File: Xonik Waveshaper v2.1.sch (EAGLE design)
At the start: 89 parts, among them IC1 TL074D, IC2 TL074D, IC3 TL074D, IC4 TL072D, IC5 4013D, T1 2n3904

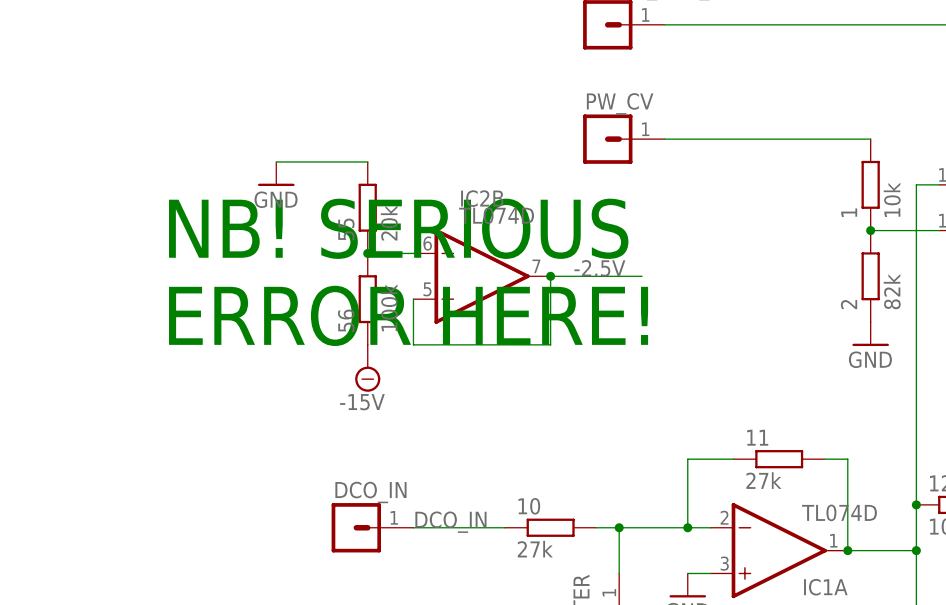
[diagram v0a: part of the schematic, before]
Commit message: v2.1 - fixed serious bug, had mixed up + and - on -2.5v generator op amp
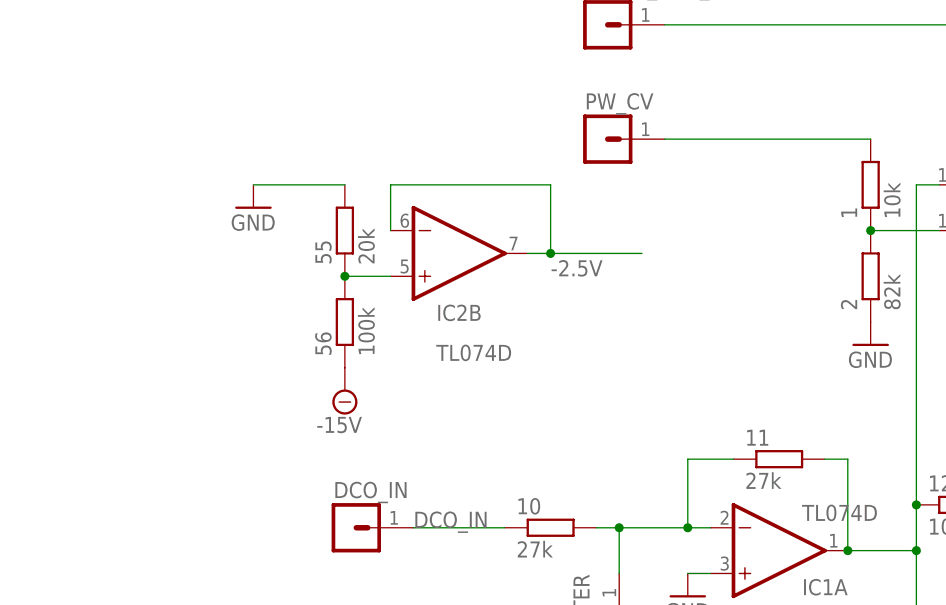
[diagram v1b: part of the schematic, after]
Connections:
- net -2.5V: now also IC2B.-IN; no longer IC2B.+IN
- net N$33: now also IC2B.+IN; no longer IC2B.-IN
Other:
- note removed: "NB! SERIOUS ERROR HERE!"
- moved on the sheet: 55, 56, IC2B
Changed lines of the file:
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@@
 <text x="-48.26" y="111.76" size="1.778" layer="97">PW is about 6% of the total cycle at the narrowest.
 Change R2 to 150 to reduce to half that.</text>
-<text x="-83.82" y="68.58" size="6.4516" layer="91">NB! SERIOUS
-ERROR HERE!</text>
 </plain>
 <instances>
@@
 <attribute name="VALUE" x="25.4" y="-81.28" size="1.778" layer="96" rot="MR180"/>
 </instance>
-<instance part="IC2" gate="B" x="-48.26" y="76.2" smashed="yes" rot="MR180">
-<attribute name="NAME" x="-50.8" y="85.725" size="1.778" layer="95" rot="MR180"/>
-<attribute name="VALUE" x="-50.8" y="83.82" size="1.778" layer="96" rot="MR180"/>
+<instance part="IC2" gate="B" x="-50.8" y="78.74" smashed="yes" rot="MR180">
+<attribute name="NAME" x="-53.34" y="73.025" size="1.778" layer="95" rot="MR180"/>
+<attribute name="VALUE" x="-53.34" y="68.58" size="1.778" layer="96" rot="MR180"/>
 </instance>
 <instance part="IC4" gate="B" x="22.86" y="-20.32" smashed="yes" rot="MR180">
@@
 <attribute name="VALUE" x="53.34" y="-114.3" size="1.778" layer="96"/>
 </instance>
-<instance part="55" gate="G$1" x="-60.96" y="83.82" smashed="yes" rot="R90">
-<attribute name="NAME" x="-62.4586" y="80.01" size="1.778" layer="95" rot="R90"/>
-<attribute name="VALUE" x="-57.658" y="80.01" size="1.778" layer="96" rot="R90"/>
-</instance>
-<instance part="56" gate="G$1" x="-60.96" y="73.66" smashed="yes" rot="R90">
-<attribute name="NAME" x="-62.4586" y="69.85" size="1.778" layer="95" rot="R90"/>
-<attribute name="VALUE" x="-57.658" y="69.85" size="1.778" layer="96" rot="R90"/>
-</instance>
-<instance part="SUPPLY2" gate="G$1" x="-60.96" y="66.04" smashed="yes">
-<attribute name="VALUE" x="-64.135" y="61.341" size="1.778" layer="96"/>
-</instance>
-<instance part="GND14" gate="1" x="-71.12" y="86.36" smashed="yes">
-<attribute name="VALUE" x="-73.66" y="83.82" size="1.778" layer="96"/>
+<instance part="55" gate="G$1" x="-63.5" y="81.28" smashed="yes" rot="R90">
+<attribute name="NAME" x="-64.9986" y="77.47" size="1.778" layer="95" rot="R90"/>
+<attribute name="VALUE" x="-60.198" y="77.47" size="1.778" layer="96" rot="R90"/>
+</instance>
+<instance part="56" gate="G$1" x="-63.5" y="71.12" smashed="yes" rot="R90">
+<attribute name="NAME" x="-64.9986" y="67.31" size="1.778" layer="95" rot="R90"/>
+<attribute name="VALUE" x="-60.198" y="67.31" size="1.778" layer="96" rot="R90"/>
+</instance>
+<instance part="SUPPLY2" gate="G$1" x="-63.5" y="63.5" smashed="yes">
+<attribute name="VALUE" x="-66.675" y="58.801" size="1.778" layer="96"/>
+</instance>
+<instance part="GND14" gate="1" x="-73.66" y="83.82" smashed="yes">
+<attribute name="VALUE" x="-76.2" y="81.28" size="1.778" layer="96"/>
 </instance>
 <instance part="IC5" gate="A" x="-35.56" y="-17.78" smashed="yes">
@@
 <pinref part="GND14" gate="1" pin="GND"/>
 <pinref part="55" gate="G$1" pin="2"/>
-<wire x1="-71.12" y1="88.9" x2="-60.96" y2="88.9" width="0.1524" layer="91"/>
+<wire x1="-73.66" y1="86.36" x2="-63.5" y2="86.36" width="0.1524" layer="91"/>
 </segment>
 <segment>
@@
 </segment>
 <segment>
-<pinref part="IC2" gate="B" pin="+IN"/>
-<wire x1="-55.88" y1="73.66" x2="-55.88" y2="68.58" width="0.1524" layer="91"/>
 <pinref part="IC2" gate="B" pin="OUT"/>
-<wire x1="-55.88" y1="68.58" x2="-40.64" y2="68.58" width="0.1524" layer="91"/>
-<wire x1="-40.64" y1="68.58" x2="-40.64" y2="76.2" width="0.1524" layer="91"/>
-<wire x1="-40.64" y1="76.2" x2="-30.48" y2="76.2" width="0.1524" layer="91"/>
-<junction x="-40.64" y="76.2"/>
-<label x="-38.1" y="76.2" size="1.778" layer="95"/>
+<wire x1="-43.18" y1="78.74" x2="-40.64" y2="78.74" width="0.1524" layer="91"/>
+<label x="-40.64" y="76.2" size="1.778" layer="95"/>
+<pinref part="IC2" gate="B" pin="-IN"/>
+<wire x1="-40.64" y1="78.74" x2="-30.48" y2="78.74" width="0.1524" layer="91"/>
+<wire x1="-58.42" y1="81.28" x2="-58.42" y2="86.36" width="0.1524" layer="91"/>
+<wire x1="-58.42" y1="86.36" x2="-40.64" y2="86.36" width="0.1524" layer="91"/>
+<wire x1="-40.64" y1="86.36" x2="-40.64" y2="78.74" width="0.1524" layer="91"/>
+<junction x="-40.64" y="78.74"/>
 </segment>
 </net>
@@
 <pinref part="55" gate="G$1" pin="1"/>
 <pinref part="56" gate="G$1" pin="2"/>
-<pinref part="IC2" gate="B" pin="-IN"/>
-<wire x1="-55.88" y1="78.74" x2="-60.96" y2="78.74" width="0.1524" layer="91"/>
-<junction x="-60.96" y="78.74"/>
-</segment>
-</net>
+<pinref part="IC2" gate="B" pin="+IN"/>
+<wire x1="-58.42" y1="76.2" x2="-63.5" y2="76.2" width="0.1524" layer="91"/>
+<junction x="-63.5" y="76.2"/>
+</segment>
+</net>

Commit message: Replaced 1.5k R19 with 1.2k for a sine closer to +/-5v
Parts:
- 19: value 1k5 -> 1k2
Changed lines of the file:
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@@
 <part name="17" library="resistor" deviceset="R-EU_" device="R0805" value="200k"/>
 <part name="18" library="resistor" deviceset="R-EU_" device="R0805" value="150k"/>
-<part name="19" library="resistor" deviceset="R-EU_" device="R0805" value="1k5"/>
+<part name="19" library="resistor" deviceset="R-EU_" device="R0805" value="1k2"/>
 <part name="20" library="resistor" deviceset="R-EU_" device="R0805" value="15k"/>
 <part name="22" library="resistor" deviceset="R-EU_" device="R0805" value="22k"/>

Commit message: will remove resistor divider
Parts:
- added -2.5V: (no value), joakim:MA01-1JP
- added 9: 50k, resistor:R-EU_R0805
- 55: value 20k -> 100k
- 56: value 100k -> 240k
- renumbered +15V to +12V, -15V to -12V
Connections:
- net +15V renamed +12V
- net -15V renamed -12V
- removed net PW_CV: 1.2, PW_CV.1
- new net N$25: 1.2, 55.2, IC2B.OUT
- new net N$8: 55.1, 56.2, 9.1, IC2B.-IN
- net -2.5V: now also -2.5V.1; no longer IC2B.-IN, IC2B.OUT
- net GND: now also IC2B.+IN; no longer 55.2
- net N$33: now also 9.2, PW_CV.1; no longer 55.1, 56.2, IC2B.+IN
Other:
- note added: "Ext 100k pot to -12V"
- note added: "Ext 47k pot GND to +12V"
- note added: "TODO: Fjerne resistor divider for å kunne bruke full CV"
- note added: "TODO: Hva skjer med amplitude her når Vcc for IC5 er 3v3, ikke 5? Burde vi ha dedikert clean 5V?"
- note added: "TODO: Remove divider before pwm comparator op amp"
- note removed: "Ext 100k pot to -15V"
- note removed: "Ext 47k pot GND to +15V"
- moved on the sheet: 55, 56, IC2B, PW_CV

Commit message: Split connector into 19p + 5p to use available from JLCPB
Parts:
- removed 1: 10k, resistor:R-EU_R0805
- removed 2: 82k, resistor:R-EU_R0805
- removed 55: 100k, resistor:R-EU_R0805
- removed 56: 240k, resistor:R-EU_R0805
- removed 9: 50k, resistor:R-EU_R0805
- removed GND27: (no value), joakim:MA01-1JP
- C3, C4: value ?pF -> 30pF
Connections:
- net N$38 renamed TRIANGLE
- removed net N$25: 1.2, 55.2, IC2B.OUT
- removed net N$8: 55.1, 56.2, 9.1, IC2B.-IN
- net -12V: no longer 56.1
- net GND: no longer 2.1
- net N$1: now also IC2B.-IN, IC2B.OUT; no longer 1.1, 2.2, IC1D.+IN
- net N$33: now also IC1D.+IN; no longer 9.2
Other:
- note added: "30pF for filtering saw wave cuts off about half the spike, but also rounds off the rest. It has a cutoff frequency of 113kHz."
- note removed: "30pF for filtering saw wave cuts off about half the spike, but also rounds off the rest. Not sure if it is worth doing."
- note removed: "NB: 330k?"
- note removed: "PW is about 6% of the total cycle at the narrowest. Change R2 to 150 to reduce to half that."
- note removed: "TODO: Fjerne resistor divider for å kunne bruke full CV"
- note removed: "TODO: Remove divider before pwm comparator op amp"
- note removed: "Timer input = ok 330k not needed."
- moved on the sheet: IC2B, PW_CV

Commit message: Changed comment about flipflop voltage
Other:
- note added: "TODO: Hvis vi skal bruke 3v3 supply på flipflop'er så må vi bytte R26 og R27 med 6.6k Evt kan vi ha dedikert clean 5V?"
- note removed: "TODO: Hva skjer med amplitude her når Vcc for IC5 er 3v3, ikke 5? Burde vi ha dedikert clean 5V?"
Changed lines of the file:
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@@
 <text x="76.2" y="114.3" size="2.54" layer="97">used to be 5pF but 5p
 is extended part, using 6p instead.</text>
-<text x="-233.68" y="-63.5" size="6.4516" layer="91">TODO: Hva skjer med amplitude her når
-Vcc for IC5 er 3v3, ikke 5?
-Burde vi ha dedikert clean 5V?</text>
+<text x="-233.68" y="-63.5" size="6.4516" layer="91">TODO:
+Hvis vi skal bruke 3v3 supply
+på flipflop'er så må vi bytte
+R26 og R27 med 6.6k
+Evt kan vi ha dedikert clean 5V?</text>
 </plain>
 <instances>

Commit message: Changed to R0603 and 3v3 operation
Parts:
- added 1, 2: 390R, rcl:R-EU_R0603
- 10, 11, 12, 13, 14, 15, 16, 17, 18, 19, 20, 23, 24, 25, 28, 29, 3, 30, 35, 36, 37, 38, 39, 4, 40, 41, 44, 45, 46, 47, 48, 49, 5, 50, 6, 7, 8: device resistor:R-EU_R0805 -> rcl:R-EU_R0603
- 26, 27: value 10k -> 6k2; device resistor:R-EU_R0805 -> rcl:R-EU_R0603
- C1, C2, C3, C4, C5, C6, C7, C8: device resistor:C-EUC0805 -> rcl:C-EUC0603
- C10, C11, C16: device resistor:C-EUC0603K -> rcl:C-EUC0603
- renumbered +5V to +3V3
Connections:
- net +5V renamed +3V3
- new net N$25: 2.2, 27.1
- new net N$8: 1.2, 26.1
- net N$32: now also 1.1; no longer 26.1
- net N$35: now also 2.1; no longer 27.1
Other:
- note added: "TODO: kan vi ha dedikert clean 5V?"
- note removed: "TODO: Hvis vi skal bruke 3v3 supply på flipflop'er så må vi bytte R26 og R27 med 6.6k Evt kan vi ha dedikert clean 5V?"

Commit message: Updated component values after simulation
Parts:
- removed 36, 50: 27k, rcl:R-EU_R0603
- added 21: 15k, rcl:R-EU_R0603
- added 31: 27k, rcl:R-EU_R0603
- added 9: 30k, rcl:R-EU_R0603
- 16: value 150k -> 100k
- 32, 48: value 27k -> 33k
- 35, 49: value 27k -> 100k
- 38, 39, 41, 44, 46, 47: value 47k -> 49.9k
- 40, 45: value 47k -> 33k
- 5, 8: value 20k -> 200k
- 6, 7: value 10k -> 100k
- C7: value 6pF -> 3pF
- renumbered 37 to 32
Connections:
- new net N$38: 21.1, CENTER.1
- new net N$42: 31.1, 9.2, IC2B.OUT
- net GND: no longer 36.1, 50.2
- net N$1: now also 21.2, 9.1; no longer IC2B.OUT
- net N$10: now also 31.2; no longer CENTER.1
- net N$21: now also IC3B.-IN; no longer 50.1
- net N$23: now also ST1.1; no longer 35.2, 36.2
- net N$24: now also 35.2; no longer ST1.1
- net N$28: no longer IC3B.-IN
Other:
- note added: "0-5V in = 0 to -10V out"
- note added: "Ext 50k pot"
- note added: "Ext 50k to 47k pot GND to +12V or direct to 5V CV"
- note added: "Ext direct to 5V CV or 22k to 100k pot between 0 and 12V?"
- note added: "TODO: DGND?"
- note removed: "Ext 100k pot"
- note removed: "Ext 100k pot to -12V"
- note removed: "Ext 47k pot GND to +12V"
- moved on the sheet: 2, 27, 28, 30, 35, 38, 39, 40, 41, 44, 45, 46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

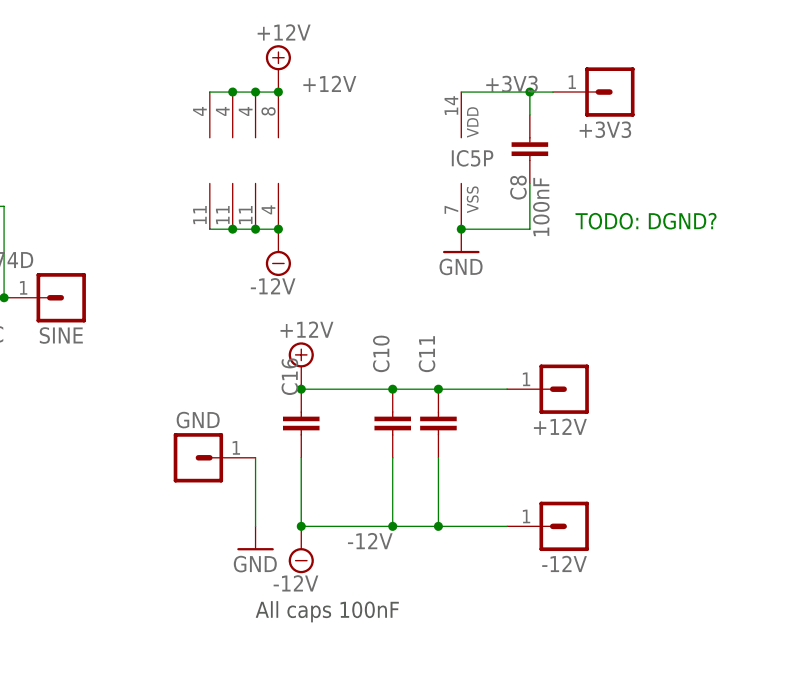
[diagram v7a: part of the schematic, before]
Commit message: Changed size and number of decoupling caps
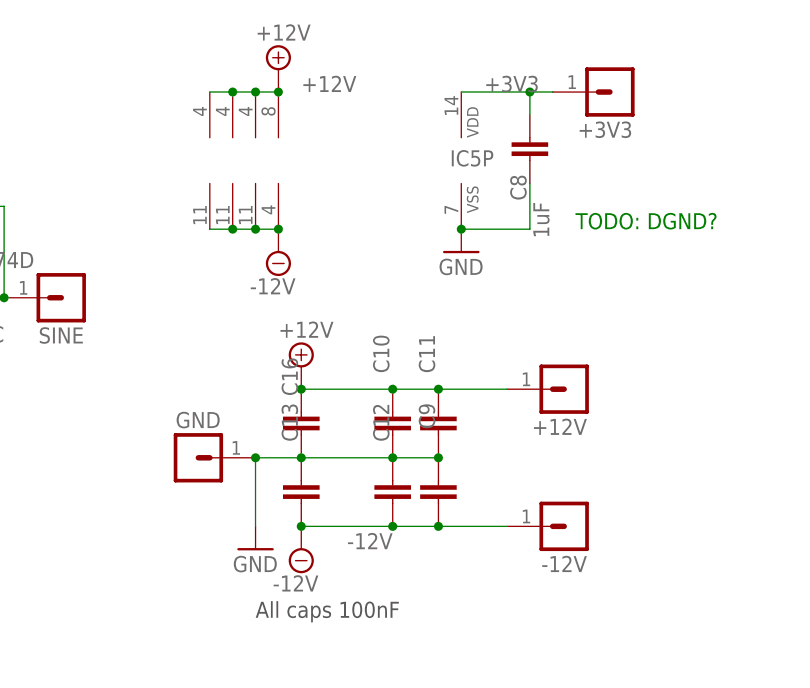
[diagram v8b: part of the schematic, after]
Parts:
- added C12, C13, C9: 1uF, rcl:C-EUC0402
- C10, C11, C16, C8: value 100nF -> 1uF; device rcl:C-EUC0603 -> rcl:C-EUC0402
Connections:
- net -12V: now also C12.1, C13.1, C9.1; no longer C10.1, C11.1, C16.1
- net GND: now also C10.1, C11.1, C12.2, C13.2, C16.1, C9.2
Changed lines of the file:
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@@
 <part name="D3" library="joakim" deviceset="1N4148" device="0805"/>
 <part name="D4" library="joakim" deviceset="1N4148" device="0805"/>
-<part name="C16" library="rcl" library_urn="urn:adsk.eagle:library:334" deviceset="C-EU" device="C0603" package3d_urn="urn:adsk.eagle:package:23616/2" value="100nF"/>
-<part name="C10" library="rcl" library_urn="urn:adsk.eagle:library:334" deviceset="C-EU" device="C0603" package3d_urn="urn:adsk.eagle:package:23616/2" value="100nF"/>
-<part name="C11" library="rcl" library_urn="urn:adsk.eagle:library:334" deviceset="C-EU" device="C0603" package3d_urn="urn:adsk.eagle:package:23616/2" value="100nF"/>
-<part name="C8" library="rcl" library_urn="urn:adsk.eagle:library:334" deviceset="C-EU" device="C0603" package3d_urn="urn:adsk.eagle:package:23616/2" value="100nF"/>
+<part name="C16" library="rcl" library_urn="urn:adsk.eagle:library:334" deviceset="C-EU" device="C0402" package3d_urn="urn:adsk.eagle:package:23626/2" value="1uF"/>
+<part name="C10" library="rcl" library_urn="urn:adsk.eagle:library:334" deviceset="C-EU" device="C0402" package3d_urn="urn:adsk.eagle:package:23626/2" value="1uF"/>
+<part name="C11" library="rcl" library_urn="urn:adsk.eagle:library:334" deviceset="C-EU" device="C0402" package3d_urn="urn:adsk.eagle:package:23626/2" value="1uF"/>
+<part name="C8" library="rcl" library_urn="urn:adsk.eagle:library:334" deviceset="C-EU" device="C0402" package3d_urn="urn:adsk.eagle:package:23626/2" value="1uF"/>
 <part name="PULSE" library="joakim" deviceset="MA01-1J" device="P"/>
 <part name="SINE" library="joakim" deviceset="MA01-1J" device="P"/>
@@
 <part name="21" library="rcl" library_urn="urn:adsk.eagle:library:334" deviceset="R-EU_" device="R0603" package3d_urn="urn:adsk.eagle:package:23555/3" value="15k"/>
 <part name="32" library="rcl" library_urn="urn:adsk.eagle:library:334" deviceset="R-EU_" device="R0603" package3d_urn="urn:adsk.eagle:package:23555/3" value="33k"/>
+<part name="C9" library="rcl" library_urn="urn:adsk.eagle:library:334" deviceset="C-EU" device="C0402" package3d_urn="urn:adsk.eagle:package:23626/2" value="1uF"/>
+<part name="C12" library="rcl" library_urn="urn:adsk.eagle:library:334" deviceset="C-EU" device="C0402" package3d_urn="urn:adsk.eagle:package:23626/2" value="1uF"/>
+<part name="C13" library="rcl" library_urn="urn:adsk.eagle:library:334" deviceset="C-EU" device="C0402" package3d_urn="urn:adsk.eagle:package:23626/2" value="1uF"/>
 </parts>
 <sheets>
@@
 <attribute name="VALUE" x="11.43" y="-38.862" size="1.778" layer="96"/>
 </instance>
+<instance part="C9" gate="G$1" x="149.86" y="35.56" smashed="yes" rot="R180">
+<attribute name="NAME" x="147.701" y="46.736" size="1.778" layer="95" rot="R270"/>
+</instance>
+<instance part="C12" gate="G$1" x="144.78" y="35.56" smashed="yes" rot="R180">
+<attribute name="NAME" x="142.621" y="46.736" size="1.778" layer="95" rot="R270"/>
+</instance>
+<instance part="C13" gate="G$1" x="134.62" y="35.56" smashed="yes" rot="R180">
+<attribute name="NAME" x="132.461" y="46.736" size="1.778" layer="95" rot="R270"/>
+</instance>
 </instances>
 <busses>
@@
 <pinref part="GND28" gate="1" pin="GND"/>
 <wire x1="129.54" y1="40.64" x2="129.54" y2="33.02" width="0.1524" layer="91"/>
+<pinref part="C11" gate="G$1" pin="1"/>
+<pinref part="C9" gate="G$1" pin="2"/>
+<wire x1="129.54" y1="40.64" x2="134.62" y2="40.64" width="0.1524" layer="91"/>
+<junction x="129.54" y="40.64"/>
+<junction x="149.86" y="40.64"/>
+<pinref part="C10" gate="G$1" pin="1"/>
+<pinref part="C12" gate="G$1" pin="2"/>
+<junction x="144.78" y="40.64"/>
+<wire x1="134.62" y1="40.64" x2="144.78" y2="40.64" width="0.1524" layer="91"/>
+<wire x1="144.78" y1="40.64" x2="149.86" y2="40.64" width="0.1524" layer="91"/>
+<pinref part="C16" gate="G$1" pin="1"/>
+<pinref part="C13" gate="G$1" pin="2"/>
+<junction x="134.62" y="40.64"/>
 </segment>
 <segment>
@@
 <pinref part="-12V" gate="G$1" pin="1"/>
 <wire x1="134.62" y1="33.02" x2="144.78" y2="33.02" width="0.1524" layer="91"/>
+<pinref part="SUPPLY11" gate="G$1" pin="-12V"/>
+<label x="139.7" y="30.48" size="1.778" layer="95"/>
+<pinref part="C13" gate="G$1" pin="1"/>
+<junction x="134.62" y="33.02"/>
+<pinref part="C12" gate="G$1" pin="1"/>
 <wire x1="144.78" y1="33.02" x2="149.86" y2="33.02" width="0.1524" layer="91"/>
+<junction x="144.78" y="33.02"/>
+<pinref part="C9" gate="G$1" pin="1"/>
 <wire x1="149.86" y1="33.02" x2="157.48" y2="33.02" width="0.1524" layer="91"/>
-<pinref part="C16" gate="G$1" pin="1"/>
-<wire x1="134.62" y1="40.64" x2="134.62" y2="33.02" width="0.1524" layer="91"/>
-<pinref part="C10" gate="G$1" pin="1"/>
-<wire x1="144.78" y1="40.64" x2="144.78" y2="33.02" width="0.1524" layer="91"/>
-<junction x="144.78" y="33.02"/>
-<pinref part="C11" gate="G$1" pin="1"/>
-<wire x1="149.86" y1="40.64" x2="149.86" y2="33.02" width="0.1524" layer="91"/>
 <junction x="149.86" y="33.02"/>
-<pinref part="SUPPLY11" gate="G$1" pin="-12V"/>
-<junction x="134.62" y="33.02"/>
-<label x="139.7" y="30.48" size="1.778" layer="95"/>
-</segment>
-</net>
+</segment>
+</net>
